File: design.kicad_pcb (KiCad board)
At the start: 2 copper layers, 40.2 x 40.2 mm, 0 parts

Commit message: init
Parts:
- added H1: MountingHole, MountingHole:MountingHole_2.7mm_M2.5_ISO7380_Pad, F.Cu at (140.0, 106.0)
- added J1: BM04B-SRSS-TB_LF__SN_, Snapeda:BM04B-SRSS-TB_LF__SN__JST_BM04B-SRSS-TB_LF__SN_, F.Cu at (133.3, 106.0)
- added J2: BM04B-SRSS-TB_LF__SN_, Snapeda:BM04B-SRSS-TB_LF__SN__JST_BM04B-SRSS-TB_LF__SN_, B.Cu at (133.3, 106.0)
- added SW1: SW_Push, Snapeda:B3F-4055_SW_B3F-4055, F.Cu at (138.2, 96.5)
- added SW2: SW_Push, Snapeda:B3F-4055_SW_B3F-4055, F.Cu at (138.2, 115.5)
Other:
- board size 40.2 x 40.2 mm -> 12.5 x 28 mm

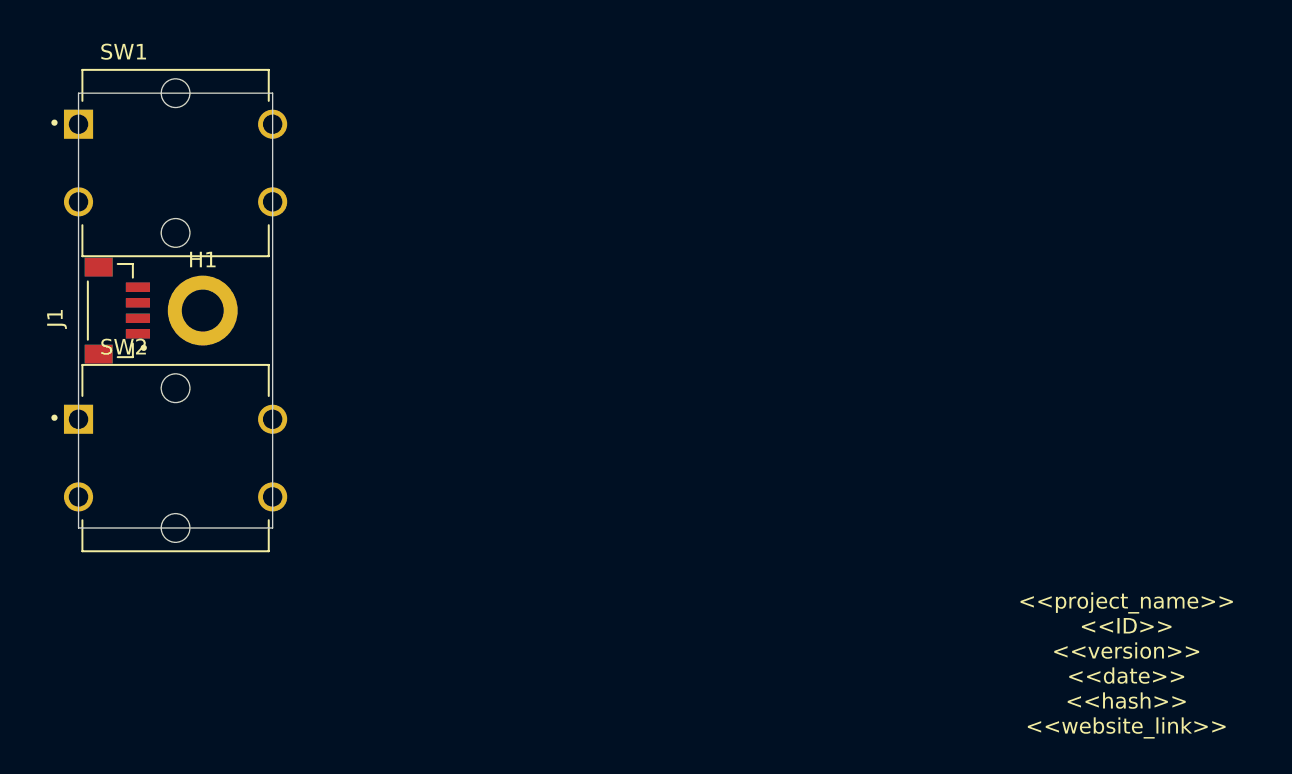
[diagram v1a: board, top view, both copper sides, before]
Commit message: cahnge to kicad 9.x and updates
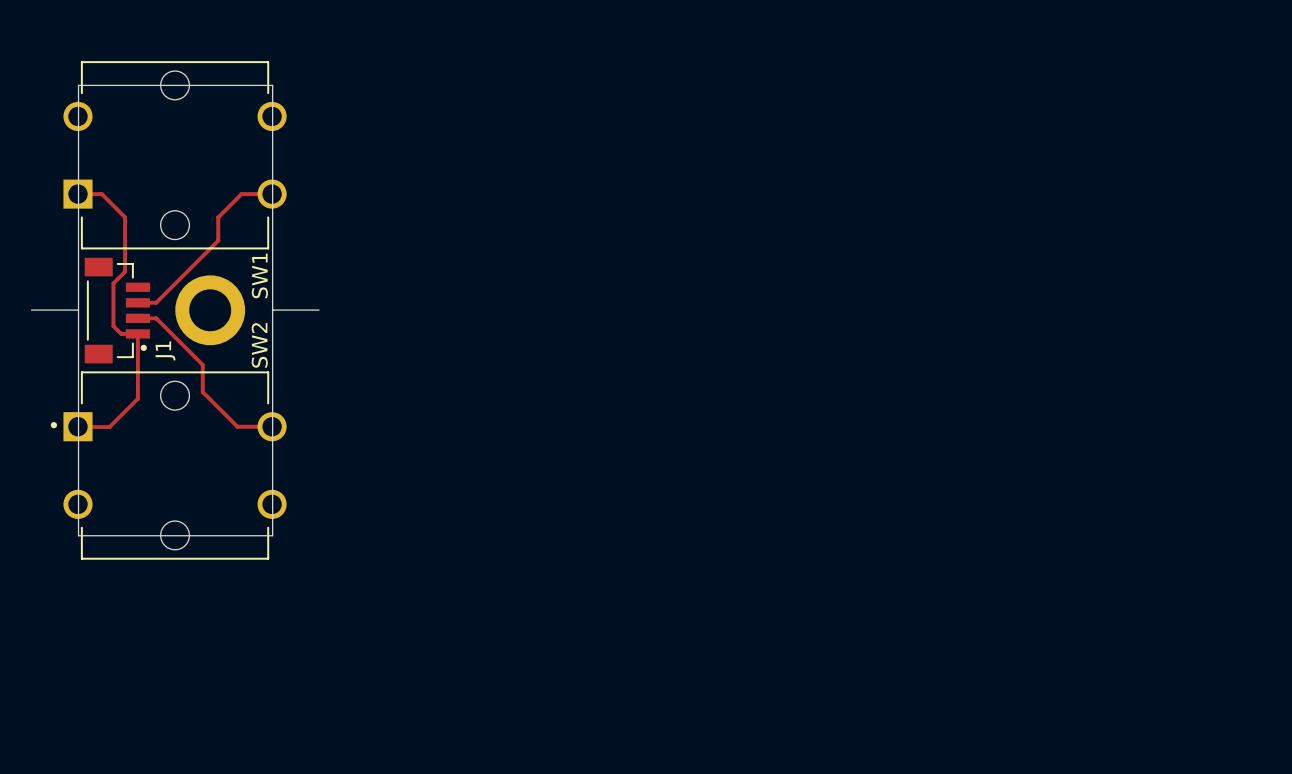
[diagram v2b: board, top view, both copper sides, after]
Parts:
- removed J2: BM04B-SRSS-TB_LF__SN_, Snapeda:BM04B-SRSS-TB_LF__SN__JST_BM04B-SRSS-TB_LF__SN_
- SW1: moved to B.Cu
- moved SW1 0.50 mm to (138.2, 96.0)
- moved SW2 0.48 mm to (138.2, 116.0)
- moved H1 0.48 mm to (140.5, 106.0)
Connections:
- J1 pad S1: unconnected-(J1-PadS1) -> unconnected-(J1-SHIELD-PadS1)
- J1 pad S2: unconnected-(J1-PadS1) -> unconnected-(J1-SHIELD-PadS1)_1
- SW1 pad 2: B1 -> B2
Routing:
- net VCC: track 0.00 -> 21.2 mm
- net B1: track 0.00 -> 12.4 mm
- net B2: track 0.00 -> 12.3 mm
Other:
- board size 12.5 x 28 mm -> 18.5 x 29 mm
- board text added: "<<ID>> <<version>>"
- board text added: "<<date>> <<hash>>"
- board text added: "<<project_name>>"
- board text removed: "<<project_name>> <<ID>> <<version>> <<date>> <<hash>> <<website_link>>"

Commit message: update
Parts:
- added J2: SM04B-SRSS-TB_LF__SN_, Connector_JST:JST_SH_SM04B-SRSS-TB_1x04-1MP_P1.00mm_Horizontal, B.Cu at (135.2, 106.0)
- moved H1 0.27 mm to (140.7, 106.0)
- moved J1 0.05 mm to (133.2, 106.0)
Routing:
- net VCC: track 21.2 -> 25.6 mm, vias 0 -> 1
- net GND: vias 0 -> 8
- net B2: vias 0 -> 1
- net B1: vias 0 -> 1
- added copper zone on B.Cu, net GND
- added copper zone on F.Cu, net GND
